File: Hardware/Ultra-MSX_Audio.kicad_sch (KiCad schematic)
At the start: 26 parts, among them J16 Waveblaster_header_02x13, J17 X2GS, U23 S29GL128S90TFI010, U24 FXMA108, U25 FXMA108, U26 FXMA108, U27 FXMA108, U4 YM2610, U9 DAC_YM3016

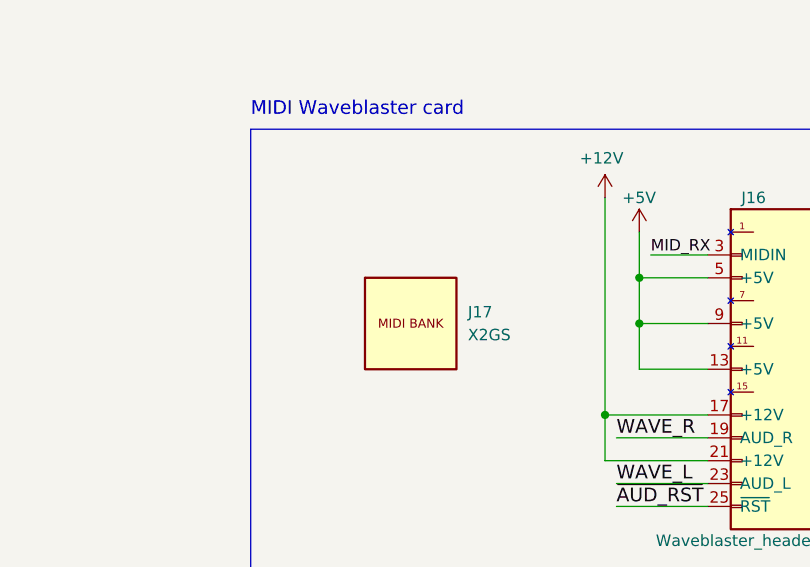
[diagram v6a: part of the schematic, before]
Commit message: Added cooler and CPU-mount footprints, as well as Indication LEDs.
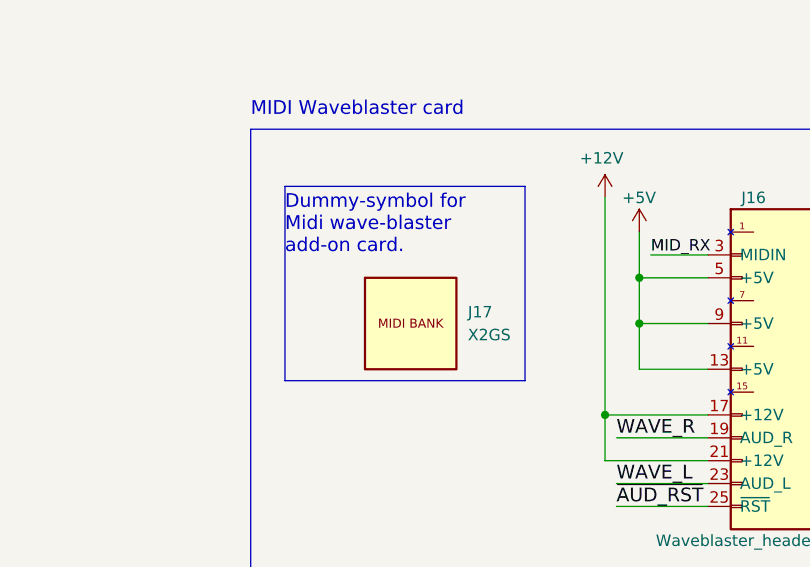
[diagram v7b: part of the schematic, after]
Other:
- note added: "Dummy-symbol for Midi wave-blaster add-on card."
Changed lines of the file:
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@@
+    (stroke (width 0) (type default) (color 0 0 0 0))
+  )
+  (polyline (pts (xy 24.13 171.45) (xy 24.13 193.04))
     (stroke (width 0) (type default) (color 0 0 0 0))
   )
@@
     (stroke (width 0) (type default) (color 0 0 0 0))
   )
+  (polyline (pts (xy 24.13 193.04) (xy 50.8 193.04))
+    (stroke (width 0) (type default) (color 0 0 0 0))
+  )
   (wire (pts (xy 344.805 158.75) (xy 344.805 154.94))
     (stroke (width 0) (type default) (color 0 0 0 0))
@@
     (stroke (width 0.5) (type solid) (color 0 0 0 0))
   )
+  (polyline (pts (xy 24.13 171.45) (xy 50.8 171.45))
+    (stroke (width 0) (type default) (color 0 0 0 0))
+  )
   (wire (pts (xy 59.69 201.93) (xy 71.12 201.93))
     (stroke (width 0) (type default) (color 0 0 0 0))
@@
   )
   (wire (pts (xy 205.74 80.01) (xy 218.44 80.01))
+    (stroke (width 0) (type default) (color 0 0 0 0))
+  )
+  (polyline (pts (xy 50.8 193.04) (xy 50.8 171.45))
     (stroke (width 0) (type default) (color 0 0 0 0))
   )
@@
     (effects (font (size 1.524 1.524)) (justify left bottom))
   )
+  (text "Dummy-symbol for\nMidi wave-blaster\nadd-on card." (at 24.13 179.07 0)
+    (effects (font (size 1.524 1.524)) (justify left bottom))
+  )

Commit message: Started fixing many small issues.
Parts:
- removed C23, C27: C_Small, Capacitor_SMD:C_0603_1608Metric, symbol Device:C_Small
- removed R24: R, Resistor_SMD:R_0603_1608Metric, symbol Device:R
- added C23, C27: C_K222K10X7RF5UH5, LRJ:C_Rect_L3.6mm_W2.3mm_P5.08mm, symbol LRJ-parts:C_GRM1885C1H222
- added R36: R_CRG0603F470R, Resistor_SMD:R_0603_1608Metric, symbol LRJ-parts:R_CRG0603F470R
- J17: value X2GS -> X2GS_midi_card; symbol Ultra-MSX:X2GS -> Ultra-MSX:X2GS_midi_card
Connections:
- net GNDA is gone; now on net GND: J16.16 (GNDA), J16.18 (GNDA), J16.20 (GNDA), J16.22 (GNDA), J16.24 (GNDA), J16.26 (GNDA)
- net ~{RESET} is gone; now on net ~{AUD_RST}: U25.6 (A4)
- net FMA-CH1_L: now also C27.1
- net FMA-CH2_R: now also C23.1
- net GND: now also C23.2, C27.2, R36.2
- net PSG_SND: now also R36.1
- net VT_~{RY/BY} renamed VT_~{RY_BY}
- net ~{RY/BY} renamed ~{RY_BY}
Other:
- note added: "MIDI Waveblaster header"
- note removed: "MIDI Waveblaster card"
